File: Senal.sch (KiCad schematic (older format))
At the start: 20 parts, among them IC1 AG849, IC2 AD5933, IC5 AD8606, P1 GSG-RF-CONN, P2 GSG-RF-CONN, P3 CONN_02X04, P4 CONN_01X01, U1 AD8606

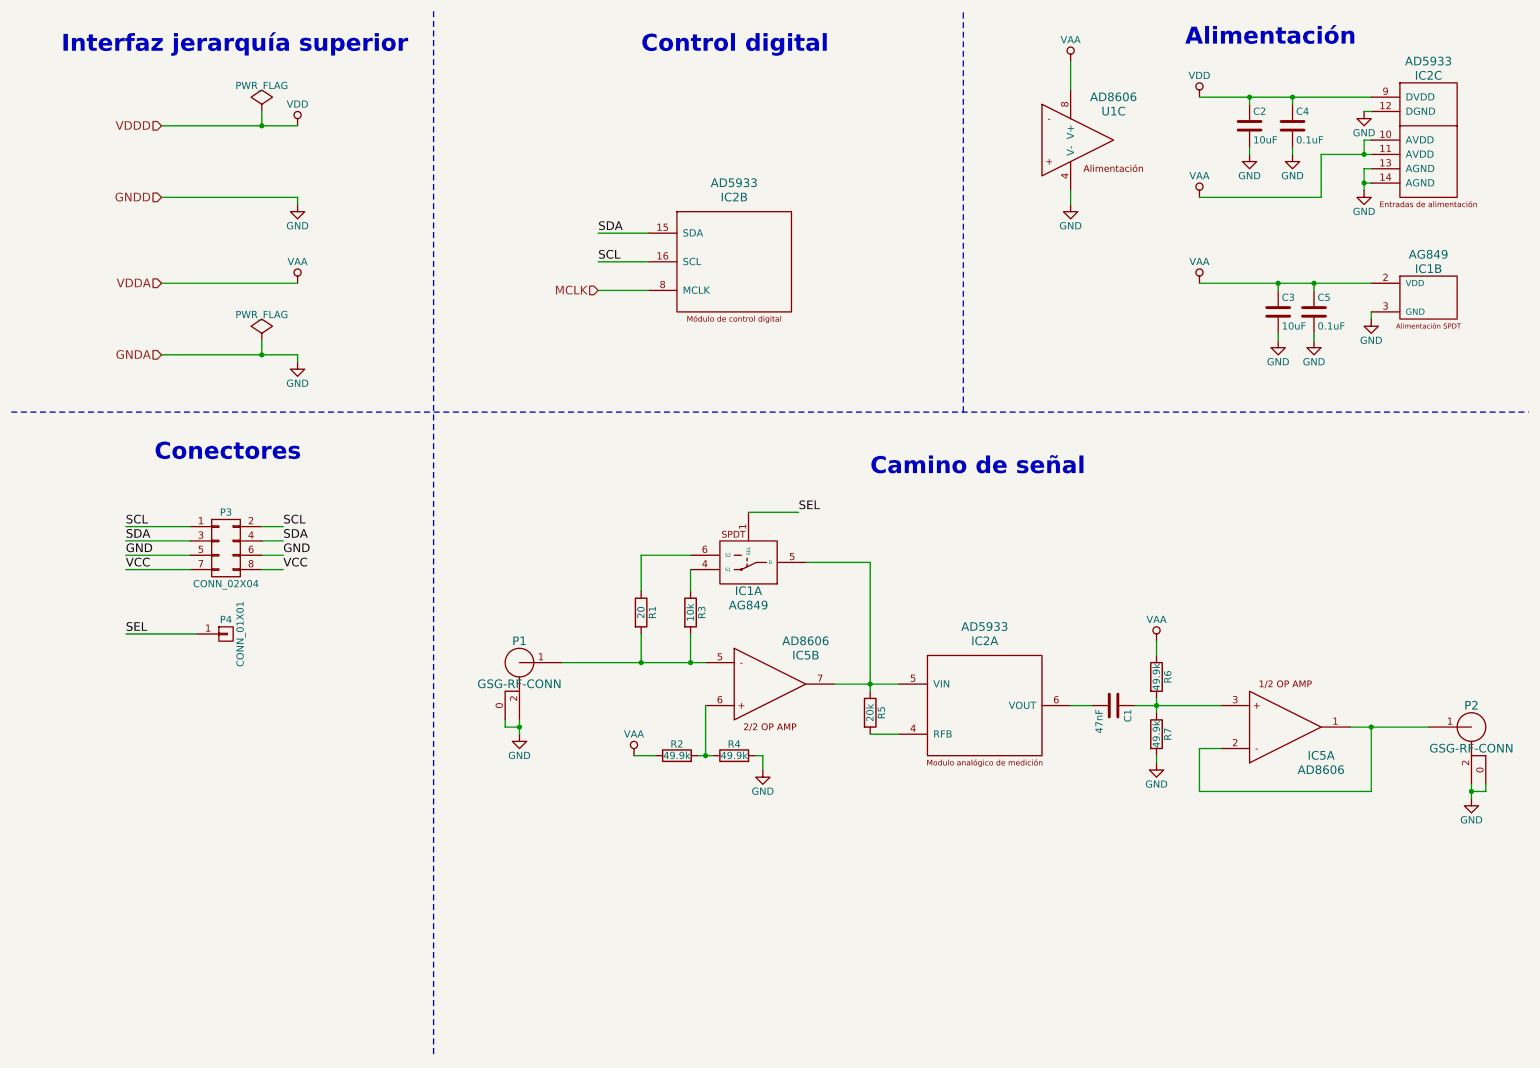
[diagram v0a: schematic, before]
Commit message: Se agregaron los campos Digikey#
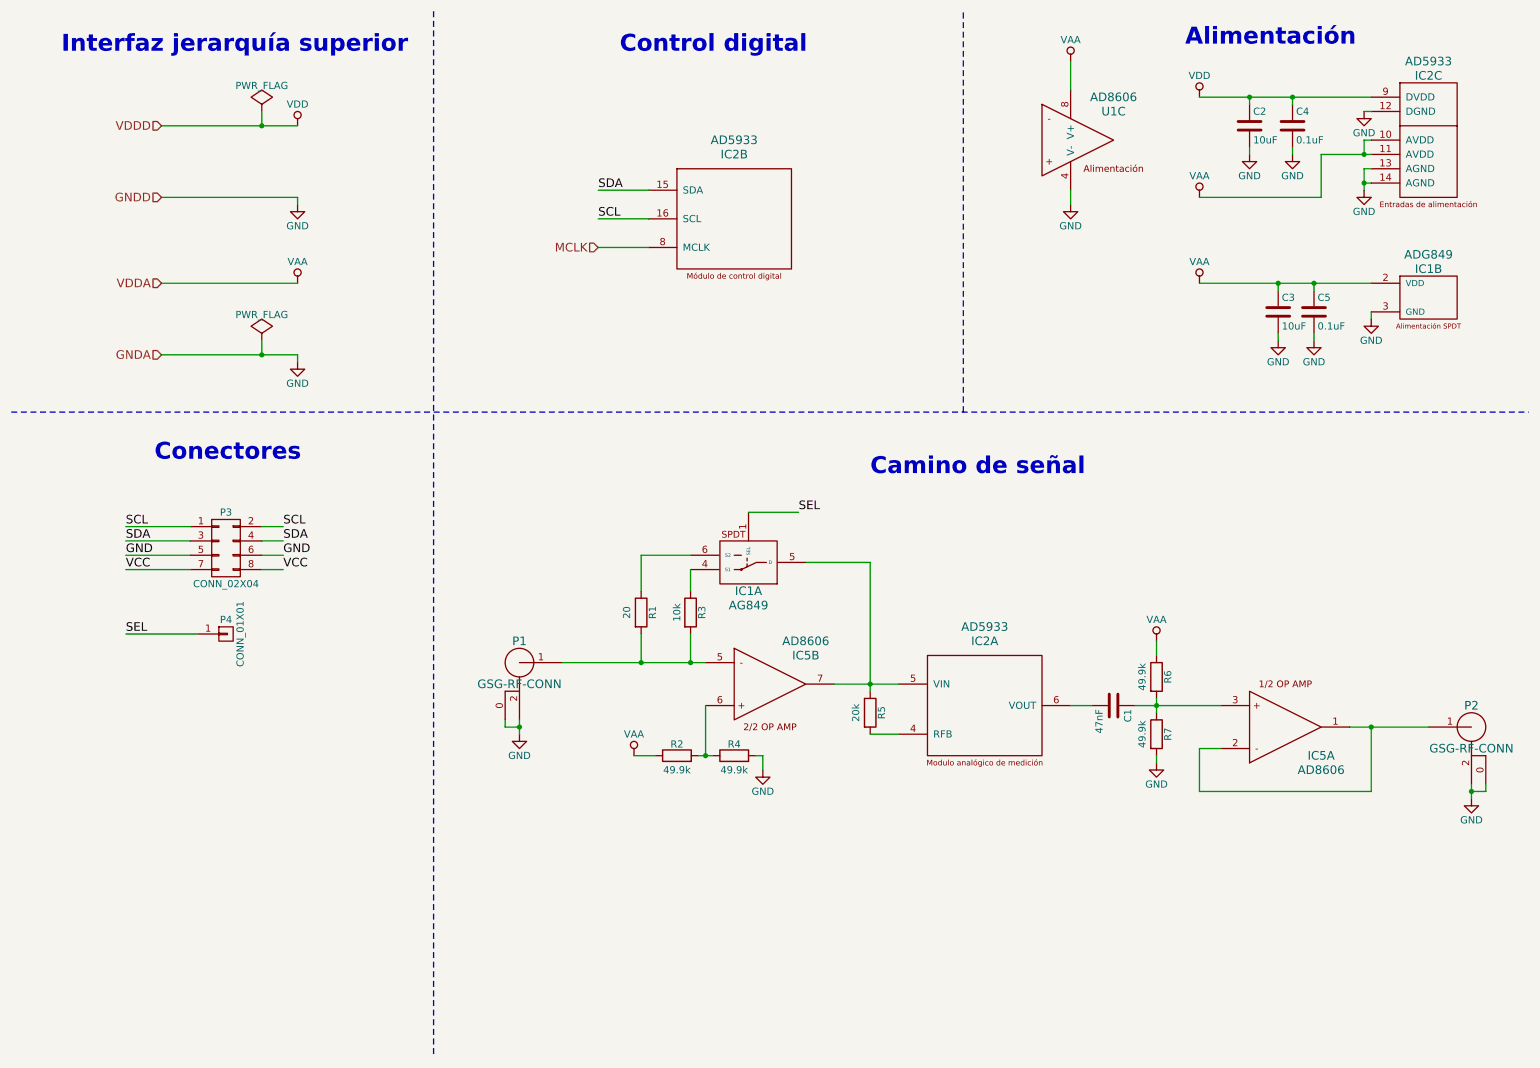
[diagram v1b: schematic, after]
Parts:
- C1: Digikey# (none) -> 478-1215-1-ND
- IC1: value AG849 -> ADG849; Digikey# (none) -> ADG849YKSZ-REEL7CT-ND
- IC1: Digikey# (none) -> ADG849YKSZ-REEL7CT-ND
- IC2: Digikey# (none) -> AD5933YRSZ-ND
- IC2: Digikey# (none) -> AD5933YRSZ-REEL7CT-ND
- IC5, U1: Digikey# (none) -> AD8606ARZ-ND
- P2: Digikey# (none) -> WM5534-ND
- P3: Digikey# (none) -> 609-3353-ND
- P4: Digikey# (none) -> 732-5314-ND
- R1, R2, R3, R4, R5, R6, R7: Digikey# (none) -> 311-10KGRTR-ND
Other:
- moved on the sheet: IC2B
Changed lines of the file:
@@
 Text HLabel 1600 2900 0    60   Input ~ 0
 GNDA
-Text HLabel 4650 2450 0    60   Input ~ 0
+Text HLabel 4650 2150 0    60   Input ~ 0
 MCLK
 $Comp
@@
 L AD5933 IC2
 U 2 1 582F78D1
-P 5600 2250
-F 0 "IC2" H 5600 2700 60  0000 C CNN
-F 1 "AD5933" H 5600 2800 60  0000 C CNN
-F 2 "Housings_SSOP:SSOP-16_5.3x6.2mm_Pitch0.65mm" H 5600 2250 60  0001 C CNN
-F 3 "" H 5600 2250 60  0001 C CNN
-	2    5600 2250
+P 5600 1950
+F 0 "IC2" H 5600 2400 60  0000 C CNN
+F 1 "AD5933" H 5600 2500 60  0000 C CNN
+F 2 "Housings_SSOP:SSOP-16_5.3x6.2mm_Pitch0.65mm" H 5600 1950 60  0001 C CNN
+F 3 "" H 5600 1950 60  0001 C CNN
+F 4 "AD5933YRSZ-ND" H 5600 1950 60  0001 C CNN "Digikey#"
+	2    5600 1950
 	1    0    0    -1
 $EndComp
@@
 F 2 "Housings_SSOP:SSOP-16_5.3x6.2mm_Pitch0.65mm" H 7350 5350 60  0001 C CNN
 F 3 "" H 7350 5350 60  0001 C CNN
+F 4 "AD5933YRSZ-REEL7CT-ND" H 7350 5350 60  0001 C CNN "Digikey#"
 	1    7350 5350
 	1    0    0    -1
@@
 F 2 "Housings_SSOP:MSOP-8_3x3mm_Pitch0.65mm" H 8000 1400 60  0001 C CNN
 F 3 "" H 8000 1400 60  0001 C CNN
+F 4 "AD8606ARZ-ND" H 8000 1400 60  0001 C CNN "Digikey#"
 	3    8000 1400
 	1    0    0    -1
@@
 P 10450 2500
 F 0 "IC1" H 10450 2700 60  0000 C CNN
-F 1 "AG849" H 10450 2800 60  0000 C CNN
+F 1 "ADG849" H 10450 2800 60  0000 C CNN
 F 2 "TO_SOT_Packages_SMD:SC-70-6" H 10450 2500 60  0001 C CNN
-F 3 "" H 10450 2500 60  0001 C CNN
+F 3 "doc/Datasheets/ADG849 (SPDT).pdf" H 10450 2500 60  0001 C CNN
+F 4 "ADG849YKSZ-REEL7CT-ND" H 10450 2500 60  0001 C CNN "Digikey#"
 	2    10450 2500
 	1    0    0    -1
@@
 F 2 "Housings_SSOP:MSOP-8_3x3mm_Pitch0.65mm" H 5850 5200 60  0001 C CNN
 F 3 "" H 5850 5200 60  0001 C CNN
+F 4 "AD8606ARZ-ND" H 5850 5200 60  0001 C CNN "Digikey#"
 	2    5850 5200
 	1    0    0    -1
@@
 P 6550 5400
 F 0 "R5" V 6630 5400 50  0000 C CNN
-F 1 "20k" V 6550 5400 50  0000 C CNN
+F 1 "20k" V 6450 5400 50  0000 C CNN
 F 2 "Resistors_SMD:R_0603" V 6480 5400 50  0001 C CNN
 F 3 "" H 6550 5400 50  0000 C CNN
+F 4 "311-10KGRTR-ND" V 6550 5400 60  0001 C CNN "Digikey#"
 	1    6550 5400
 	1    0    0    -1
@@
 P 8550 5150
 F 0 "R6" V 8630 5150 50  0000 C CNN
-F 1 "49.9k" V 8550 5150 50  0000 C CNN
+F 1 "49.9k" V 8450 5150 50  0000 C CNN
 F 2 "Resistors_SMD:R_0603" V 8480 5150 50  0001 C CNN
 F 3 "" H 8550 5150 50  0000 C CNN
+F 4 "311-10KGRTR-ND" V 8550 5150 60  0001 C CNN "Digikey#"
 	1    8550 5150
 	1    0    0    -1
@@
 P 8550 5550
 F 0 "R7" V 8630 5550 50  0000 C CNN
-F 1 "49.9k" V 8550 5550 50  0000 C CNN
+F 1 "49.9k" V 8450 5550 50  0000 C CNN
 F 2 "Resistors_SMD:R_0603" V 8480 5550 50  0001 C CNN
 F 3 "" H 8550 5550 50  0000 C CNN
+F 4 "311-10KGRTR-ND" V 8550 5550 60  0001 C CNN "Digikey#"
 	1    8550 5550
 	1    0    0    -1
@@
 F 2 "Capacitors_SMD:C_0603" H 8288 5200 50  0001 C CNN
 F 3 "" H 8250 5350 50  0000 C CNN
+F 4 "478-1215-1-ND" H 8250 5350 60  0001 C CNN "Digikey#"
 	1    8250 5350
 	0    1    1    0
@@
 F 2 "SMA_EDGE:SMA_EDGE" H 10750 5500 60  0001 C CNN
 F 3 "" H 10750 5500 60  0000 C CNN
+F 4 "WM5534-ND" H 10750 5500 60  0001 C CNN "Digikey#"
 	1    10750 5500
 	-1   0    0    -1
@@
 P 5200 5700
 F 0 "R2" V 5280 5700 50  0000 C CNN
-F 1 "49.9k" V 5200 5700 50  0000 C CNN
+F 1 "49.9k" V 5100 5700 50  0000 C CNN
 F 2 "Resistors_SMD:R_0603" V 5130 5700 50  0001 C CNN
 F 3 "" H 5200 5700 50  0000 C CNN
+F 4 "311-10KGRTR-ND" V 5200 5700 60  0001 C CNN "Digikey#"
 	1    5200 5700
 	0    -1   -1   0
@@
 P 5600 5700
 F 0 "R4" V 5680 5700 50  0000 C CNN
-F 1 "49.9k" V 5600 5700 50  0000 C CNN
+F 1 "49.9k" V 5500 5700 50  0000 C CNN
 F 2 "Resistors_SMD:R_0603" V 5530 5700 50  0001 C CNN
 F 3 "" H 5600 5700 50  0000 C CNN
+F 4 "311-10KGRTR-ND" V 5600 5700 60  0001 C CNN "Digikey#"
 	1    5600 5700
 	0    -1   -1   0
@@
 F 2 "TO_SOT_Packages_SMD:SC-70-6" H 5700 4350 60  0001 C CNN
 F 3 "" H 5700 4350 60  0001 C CNN
+F 4 "ADG849YKSZ-REEL7CT-ND" H 5700 4350 60  0001 C CNN "Digikey#"
 	1    5700 4350
 	-1   0    0    1
@@
 P 5295 4700
 F 0 "R3" V 5375 4700 50  0000 C CNN
-F 1 "10k" V 5295 4700 50  0000 C CNN
+F 1 "10k" V 5200 4700 50  0000 C CNN
 F 2 "Resistors_SMD:R_0603" V 5225 4700 50  0001 C CNN
 F 3 "" H 5295 4700 50  0000 C CNN
+F 4 "311-10KGRTR-ND" V 5295 4700 60  0001 C CNN "Digikey#"
 	1    5295 4700
 	1    0    0    -1
@@
 P 4950 4700
 F 0 "R1" V 5030 4700 50  0000 C CNN
-F 1 "20" V 4950 4700 50  0000 C CNN
+F 1 "20" V 4850 4700 50  0000 C CNN
 F 2 "Resistors_SMD:R_0603" V 4880 4700 50  0001 C CNN
 F 3 "" H 4950 4700 50  0000 C CNN
+F 4 "311-10KGRTR-ND" V 4950 4700 60  0001 C CNN "Digikey#"
 	1    4950 4700
 	1    0    0    -1
@@
 Text Label 6050 4000 0    60   ~ 0
 SEL
-Text Label 4650 2050 0    60   ~ 0
+Text Label 4650 1750 0    60   ~ 0
 SDA
-Text Label 4650 2250 0    60   ~ 0
+Text Label 4650 1950 0    60   ~ 0
 SCL
 Text Notes 8750 750  0    118  ~ 24
@@
 	5700 4000 6050 4000
 Wire Wire Line
-	5000 2250 4650 2250
-Wire Wire Line
-	5000 2450 4650 2450
-Wire Wire Line
-	4650 2050 5000 2050
+	5000 1950 4650 1950
+Wire Wire Line
+	5000 2150 4650 2150
+Wire Wire Line
+	4650 1750 5000 1750
 Wire Notes Line
 	550  3300 11150 3300
@@
 Wire Wire Line
 	6105 4350 6550 4350
-Text Notes 4950 800  0    118  ~ 24
+Text Notes 4800 800  0    118  ~ 24
 Control digital
 Text Notes 6550 3750 0    118  ~ 24
@@
 F 2 "Pin_Headers:Pin_Header_Straight_2x04" H 2050 3050 50  0001 C CNN
 F 3 "" H 2050 3050 50  0000 C CNN
+F 4 "609-3353-ND" H 2050 4250 60  0001 C CNN "Digikey#"
 	1    2050 4250
 	1    0    0    -1
@@
 F 2 "Pin_Headers:Pin_Header_Straight_1x01" H 2050 4850 50  0001 C CNN
 F 3 "" H 2050 4850 50  0000 C CNN
+F 4 "732-5314-ND" H 2050 4850 60  0001 C CNN "Digikey#"
 	1    2050 4850
 	1    0    0    -1
